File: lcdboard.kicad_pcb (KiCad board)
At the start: 2 copper layers, 64 x 120.5 mm, 70 parts, among them J1 Conn_02x05_Odd_Even, J2 Conn_02x25_Counter_Clockwise, J3 Conn_02x12_Counter_Clockwise, J4 USB_B_Micro, J5 Conn_01x03, SW1 SW_Push, SW3 SW_SPST, U1 MK82FN256VLL15, U2 Serial-Flash, U3 TPS61169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

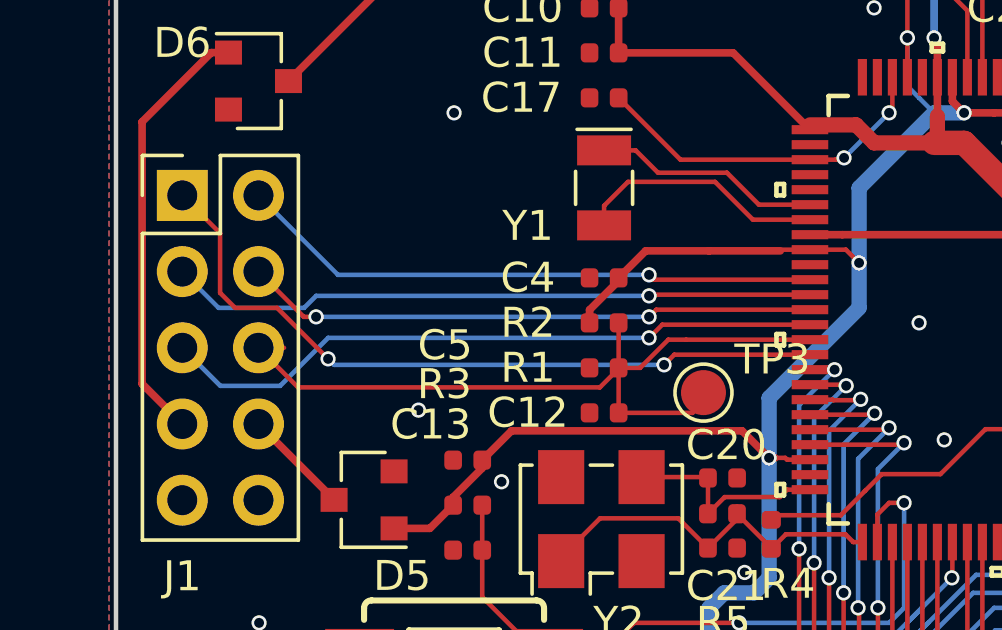
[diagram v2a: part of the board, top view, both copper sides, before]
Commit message: Add pull-up to JTAG_TRST and remove from header
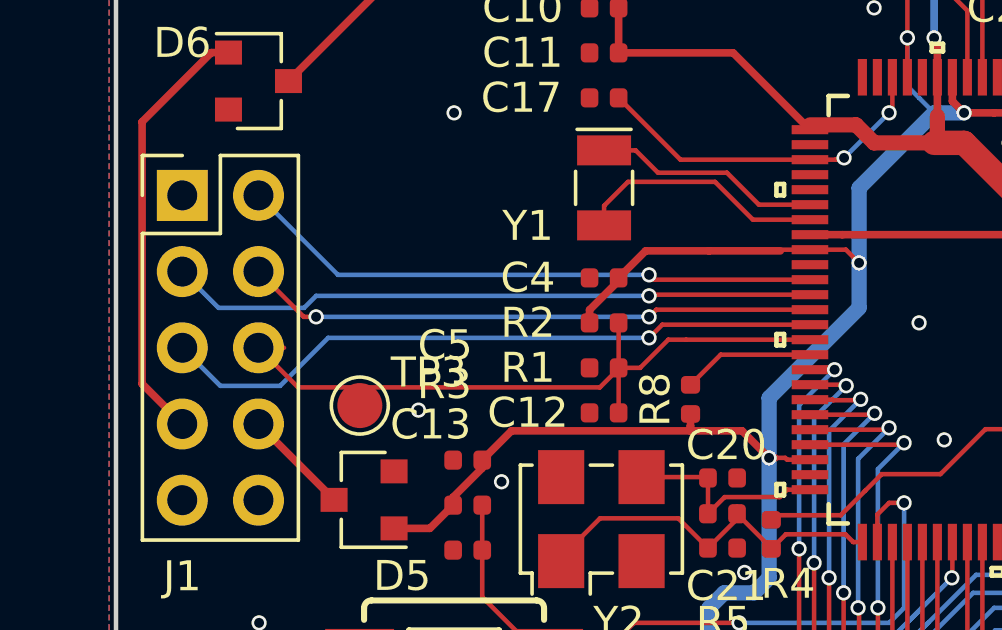
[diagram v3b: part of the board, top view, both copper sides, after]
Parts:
- added R8: 4.7K, Resistor_SMD:R_0402_1005Metric, F.Cu at (-9.12, -2.95)
- moved TP3 11.5 mm to (-20.1, -2.74)
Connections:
- J1 pad 1: /JTAG_TRST -> Net-(J1-Pad1)
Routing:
- net /JTAG_TRST: track 24.6 -> 4.40 mm, vias 2 -> 0
- net /NMI_b: track 26.7 -> 23.5 mm
- net +3V3: track 225.4 -> 225.9 mm
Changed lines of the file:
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@@
     (thickness 1.6)
     (drawings 23)
-    (tracks 1023)
+    (tracks 1015)
     (zones 0)
-    (modules 70)
-    (nets 103)
+    (modules 71)
+    (nets 104)
   )
   (page A4)
@@
     (solder_mask_min_width 0.25)
     (aux_axis_origin 0 0)
-    (visible_elements FEFFFF7F)
+    (visible_elements FEFFF77F)
     (pcbplotparams
       (layerselection 0x010fc_ffffffff)
@@
   (net 101 /EXTAL0)
   (net 102 "Net-(U1-Pad90)")
+  (net 103 "Net-(J1-Pad1)")
   (net_class Default "This is the default net class."
     (clearance 0.1524)
@@
     (add_net "Net-(D5-Pad1)")
     (add_net "Net-(D7-Pad2)")
+    (add_net "Net-(J1-Pad1)")
     (add_net "Net-(J2-Pad33)")
     (add_net "Net-(J2-Pad39)")
@@
     )
     (pad 1 thru_hole rect (at 0 0) (size 1.7 1.7) (drill 1) (layers *.Cu *.Mask)
-      (net 13 /JTAG_TRST))
+      (net 103 "Net-(J1-Pad1)"))
     (pad 2 thru_hole oval (at 2.54 0) (size 1.7 1.7) (drill 1) (layers *.Cu *.Mask)
       (net 14 /JTAG_TCLK))
@@
   )
   (module TestPoint:TestPoint_Pad_D1.5mm (layer F.Cu)
-    (at -8.6868 -3.175 180)
+    (at -20.1422 -2.7432 180)
     (descr "SMD pad as test Point, diameter 1.5mm")
     (tags "test point SMD pad")
@@
     )
   )
+  (module Resistor_SMD:R_0402_1005Metric (layer F.Cu)
+    (at -9.1186 -2.9488 90)
+    (descr "Resistor SMD 0402 (1005 Metric), square (rectangular) end terminal, IPC_7351 nominal, (Body size source: http://www.tortai-tech.com/upload/download/2011102023233369053.pdf), generated with kicad-footprint-generator")
+    (tags resistor)
+    (attr smd)
+    (fp_text reference R8 (at 0 -1.17 90) (layer F.SilkS)
+      (effects (font (size 1 1) (thickness 0.15)))
+    )
+    (fp_text value 4.7K (at 0 1.17 90) (layer F.Fab)
+      (effects (font (size 1 1) (thickness 0.15)))
+    )
+    (fp_line (start -0.5 0.25) (end -0.5 -0.25) (layer F.Fab) (width 0.1))
+    (fp_line (start -0.5 -0.25) (end 0.5 -0.25) (layer F.Fab) (width 0.1))
+    (fp_line (start 0.5 -0.25) (end 0.5 0.25) (layer F.Fab) (width 0.1))
+    (fp_line (start 0.5 0.25) (end -0.5 0.25) (layer F.Fab) (width 0.1))
+    (fp_line (start -0.93 0.47) (end -0.93 -0.47) (layer F.CrtYd) (width 0.05))
+    (fp_line (start -0.93 -0.47) (end 0.93 -0.47) (layer F.CrtYd) (width 0.05))
+    (fp_line (start 0.93 -0.47) (end 0.93 0.47) (layer F.CrtYd) (width 0.05))
+    (fp_line (start 0.93 0.47) (end -0.93 0.47) (layer F.CrtYd) (width 0.05))
+    (fp_text user %R (at 0 0 90) (layer F.Fab)
+      (effects (font (size 0.25 0.25) (thickness 0.04)))
+    )
+    (pad 1 smd roundrect (at -0.485 0 90) (size 0.59 0.64) (layers F.Cu F.Paste F.Mask) (roundrect_rratio 0.25)
+      (net 3 +3V3))
+    (pad 2 smd roundrect (at 0.485 0 90) (size 0.59 0.64) (layers F.Cu F.Paste F.Mask) (roundrect_rratio 0.25)
+      (net 13 /JTAG_TRST))
+    (model ${KISYS3DMOD}/Resistor_SMD.3dshapes/R_0402_1005Metric.wrl
+      (at (xyz 0 0 0))
+      (scale (xyz 1 1 1))
+      (rotate (xyz 0 0 0))
+    )
+  )
   (gr_text v0.1 (at -18.2 -40.6) (layer F.SilkS)
     (effects (font (size 1.5 1.5) (thickness 0.3)))
@@
   (segment (start -7.40059 -1.90059) (end -6.5 -1) (width 0.254) (layer F.Cu) (net 3))
   (segment (start -16.0616 -0.9238) (end -15.08481 -1.90059) (width 0.254) (layer F.Cu) (net 3))
-  (segment (start -15.08481 -1.90059) (end -7.40059 -1.90059) (width 0.254) (layer F.Cu) (net 3))
+  (segment (start -9.12301 -2.06439) (end -9.12301 -1.90059) (width 0.254) (layer F.Cu) (net 3))
+  (segment (start -9.1186 -2.0688) (end -9.12301 -2.06439) (width 0.254) (layer F.Cu) (net 3))
+  (segment (start -9.1186 -2.4638) (end -9.1186 -2.0688) (width 0.254) (layer F.Cu) (net 3))
+  (segment (start -15.08481 -1.90059) (end -9.12301 -1.90059) (width 0.254) (layer F.Cu) (net 3))
+  (segment (start -9.12301 -1.90059) (end -7.40059 -1.90059) (width 0.254) (layer F.Cu) (net 3))
   (via (at -14 71) (size 1.905) (drill 0.4) (layers F.Cu B.Cu) (net 4))
   (via (at -16 71) (size 1.905) (drill 0.4) (layers F.Cu B.Cu) (net 4))
@@
   (segment (start -12.139626 -3.34979) (end -22.200555 -3.34979) (width 0.1524) (layer F.Cu) (net 5))
   (segment (start -11.515 -5.5) (end -11.515 -2.5) (width 0.1524) (layer F.Cu) (net 5))
-  (segment (start -8.6868 -2.8664) (end -8.6868 -3.175) (width 0.1524) (layer F.Cu) (net 5))
-  (segment (start -11.515 -2.5) (end -9.0532 -2.5) (width 0.1524) (layer F.Cu) (net 5))
-  (segment (start -9.0532 -2.5) (end -8.6868 -2.8664) (width 0.1524) (layer F.Cu) (net 5))
   (segment (start -2.890141 1.807623) (end -2.890141 0.890141) (width 0.1524) (layer F.Cu) (net 6) (status 10))
   (via (at -2 0.5) (size 0.508) (drill 0.3302) (layers F.Cu B.Cu) (net 6))
@@
   (segment (start -27.4 -3.469235) (end -26.060142 -2.129377) (width 0.254) (layer F.Cu) (net 12) (status 20))
   (segment (start -27.4 -12.2) (end -27.4 -3.469235) (width 0.254) (layer F.Cu) (net 12))
-  (via (at -10 -4.1) (size 0.508) (drill 0.3302) (layers F.Cu B.Cu) (net 13))
-  (segment (start -5.137142 -4.439377) (end -9.660623 -4.439377) (width 0.1524) (layer F.Cu) (net 13) (status 10))
-  (segment (start -9.660623 -4.439377) (end -10 -4.1) (width 0.1524) (layer F.Cu) (net 13))
-  (via (at -21.2 -4.3) (size 0.508) (drill 0.3302) (layers F.Cu B.Cu) (net 13))
-  (segment (start -10 -4.1) (end -21 -4.1) (width 0.1524) (layer B.Cu) (net 13))
-  (segment (start -21 -4.1) (end -21.2 -4.3) (width 0.1524) (layer B.Cu) (net 13))
-  (segment (start -24.8 -8.489235) (end -26.060142 -9.749377) (width 0.1524) (layer F.Cu) (net 13) (status 20))
-  (segment (start -24.3 -6) (end -24.8 -6.5) (width 0.1524) (layer F.Cu) (net 13))
-  (segment (start -24.8 -6.5) (end -24.8 -8.489235) (width 0.1524) (layer F.Cu) (net 13))
-  (segment (start -21.2 -4.3) (end -22.9 -6) (width 0.1524) (layer F.Cu) (net 13))
-  (segment (start -22.9 -6) (end -24.3 -6) (width 0.1524) (layer F.Cu) (net 13))
+  (segment (start -8.113023 -4.439377) (end -9.1186 -3.4338) (width 0.1524) (layer F.Cu) (net 13))
+  (segment (start -5.137142 -4.439377) (end -8.113023 -4.439377) (width 0.1524) (layer F.Cu) (net 13))
   (segment (start -20.870765 -7.1) (end -23.520142 -9.749377) (width 0.1524) (layer B.Cu) (net 14) (status 20))
   (segment (start -10.5 -7.1) (end -20.870765 -7.1) (width 0.1524) (layer B.Cu) (net 14))

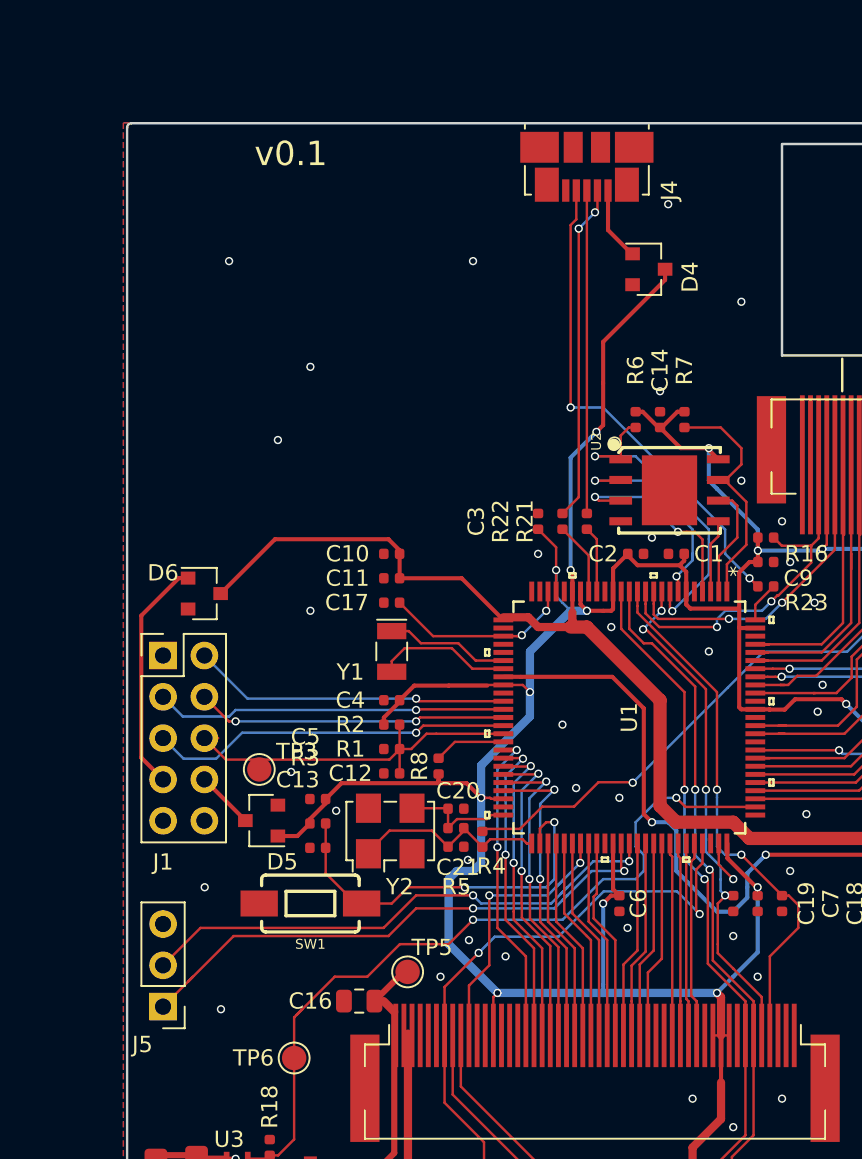
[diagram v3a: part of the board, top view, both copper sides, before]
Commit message: Rewire JTAG & UART to use 6-pin connectors
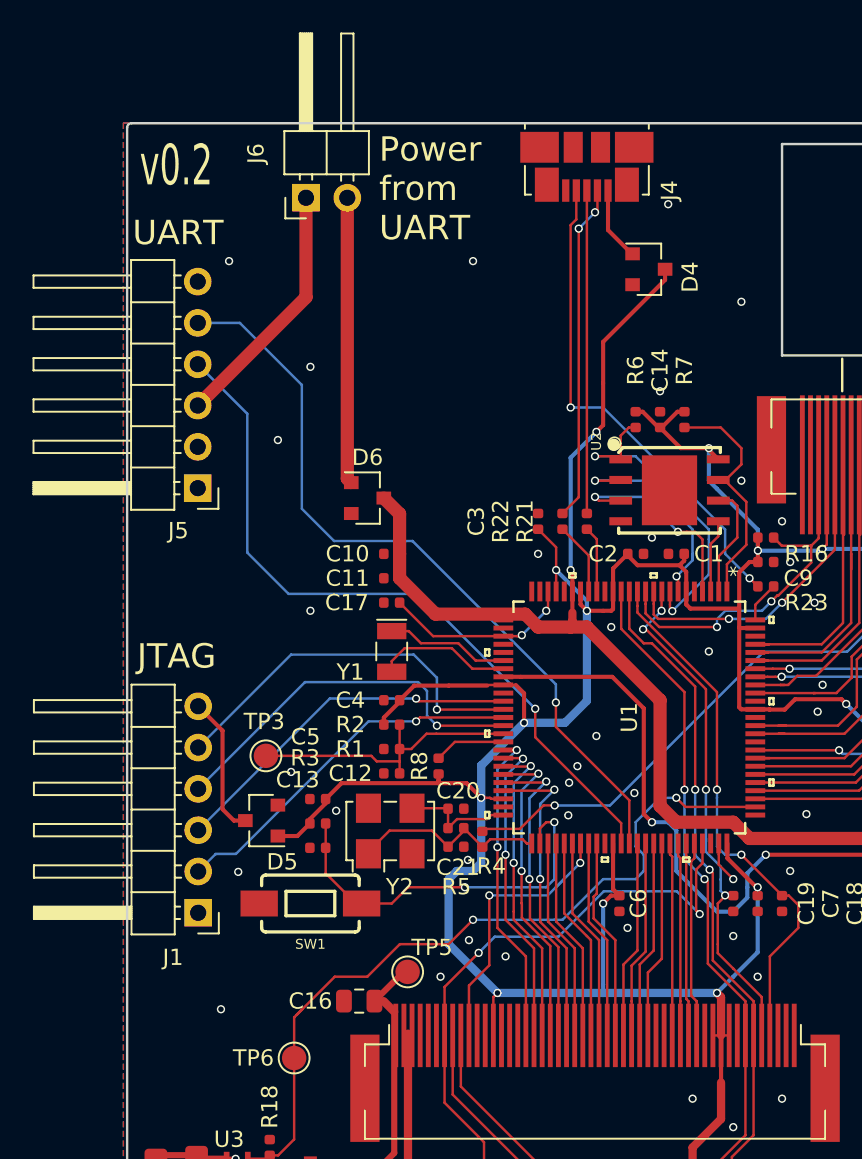
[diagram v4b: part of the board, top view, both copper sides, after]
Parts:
- added J6: Conn_01x02, Connector_PinHeader_2.54mm:PinHeader_1x02_P2.54mm_Horizontal, F.Cu at (-17.3, -37.9)
- J1: value Conn_02x05_Odd_Even -> Conn_01x06; footprint Connector_PinHeader_2.54mm:PinHeader_2x05_P2.54mm_Vertical -> Connector_PinHeader_2.54mm:PinHeader_1x06_P2.54mm_Horizontal
- J5: value Conn_01x03 -> Conn_01x06; footprint Connector_PinHeader_2.54mm:PinHeader_1x03_P2.54mm_Vertical -> Connector_PinHeader_2.54mm:PinHeader_1x06_P2.54mm_Horizontal
- moved J5 32.0 mm to (-23.9, -20.0)
- moved J1 16.0 mm to (-23.9, 6.07), turned to 180 degrees
- moved D6 11.6 mm to (-13.5, -19.4)
- moved TP3 0.93 mm to (-19.7, -3.58)
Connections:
- J1 pad 1: Net-(J1-Pad1) -> GND
- J1 pad 2: /JTAG_TCLK -> /JTAG_TDO
- J1 pad 3: /JTAG_TDI -> /JTAG_TCLK
- J1 pad 4: /JTAG_TDO -> /JTAG_TMS
- J1 pad 5: /JTAG_TMS -> /JTAG_TDI
- J1 pad 6: /NMI_b -> Net-(D5-Pad1)
- J5 pad 1: /UART_RX -> GND
- J5 pad 2: /UART_TX -> Net-(J5-Pad2)
- J5 pad 3: GND -> /+5V0
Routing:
- net /+5V0: track 0.00 -> 15.5 mm
- net /UART_TX: track 33.5 -> 47.3 mm, vias 2 -> 1
- net /UART_RX: track 34.4 -> 45.0 mm, vias 2 -> 1
- net /VDD_REGIN: track 174.6 -> 165.5 mm
- net /NMI_b: track 23.5 -> 18.1 mm
- net Net-(D5-Pad1): track 3.57 -> 8.69 mm
- net /JTAG_TDO: track 19.1 -> 22.7 mm, vias 2 -> 1
- net Net-(D6-Pad2): track 14.5 -> 17.6 mm
- net +3V3: track 225.9 -> 228.7 mm
- net /JTAG_TCLK: track 19.5 -> 22.2 mm
- net /JTAG_TDI: track 21.6 -> 23.7 mm
- net /JTAG_TMS: track 22.3 -> 23.5 mm
- net GND: vias 41 -> 43
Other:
- board text added: "CTS TX RX +5V CTS GND"
- board text added: "JTAG"
- board text added: "Power from UART"
- board text added: "UART"
- board text added: "VREF TDI TMS TCLK TDO GND"
- board text added: "v0.2"
- board text removed: "v0.1"
